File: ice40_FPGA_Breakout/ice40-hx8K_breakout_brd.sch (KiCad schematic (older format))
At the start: 0 parts

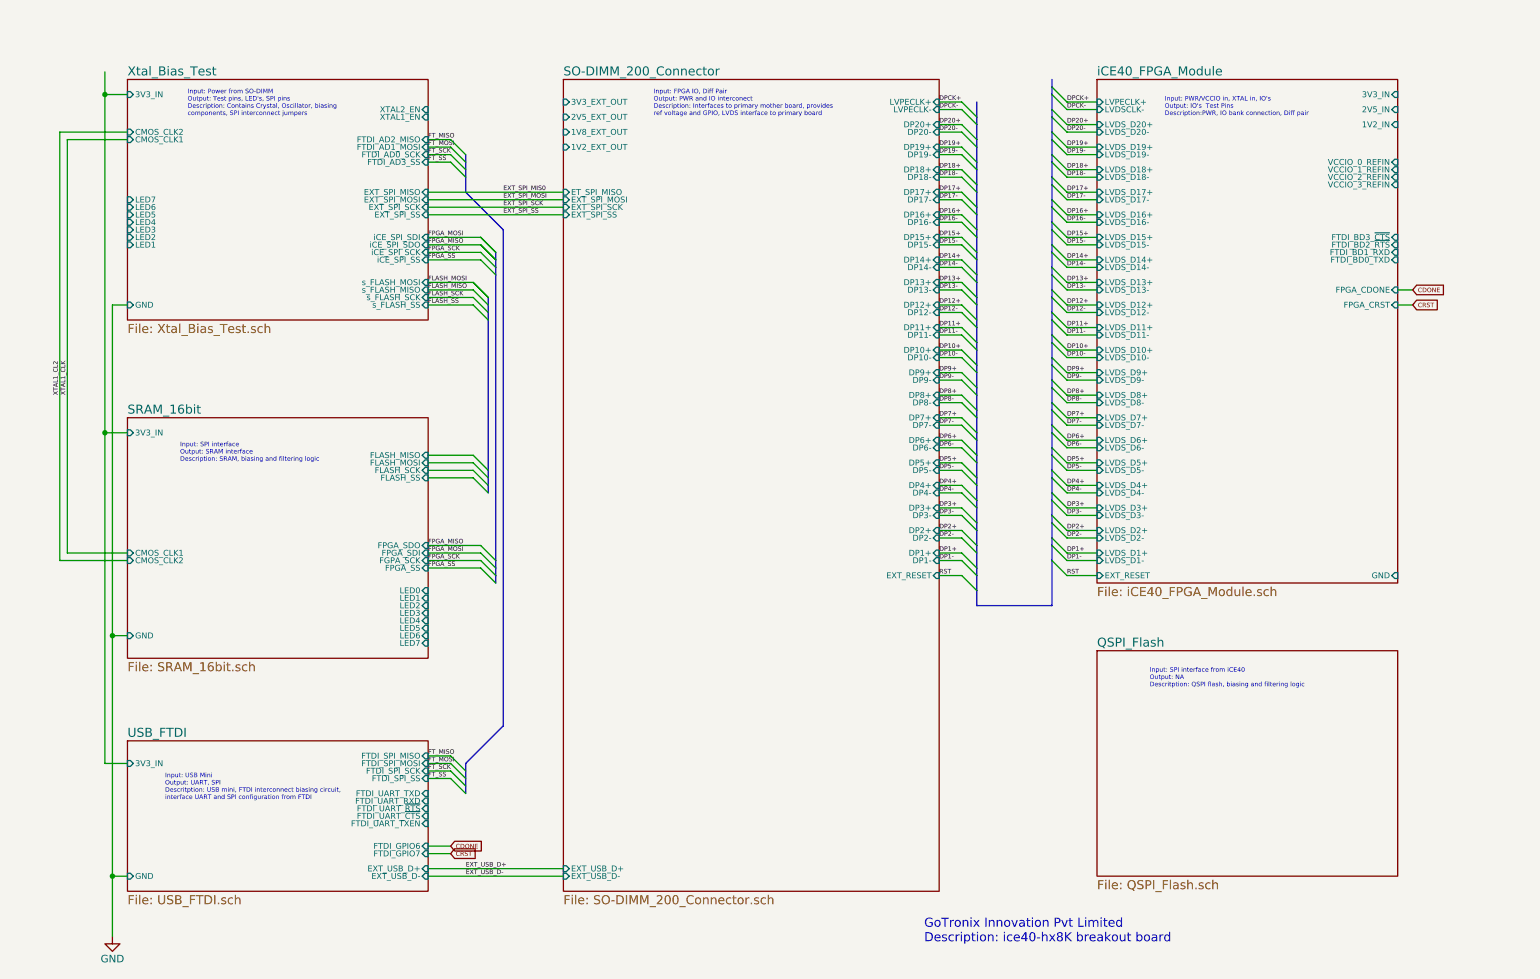
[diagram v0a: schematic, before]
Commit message: memory modules added
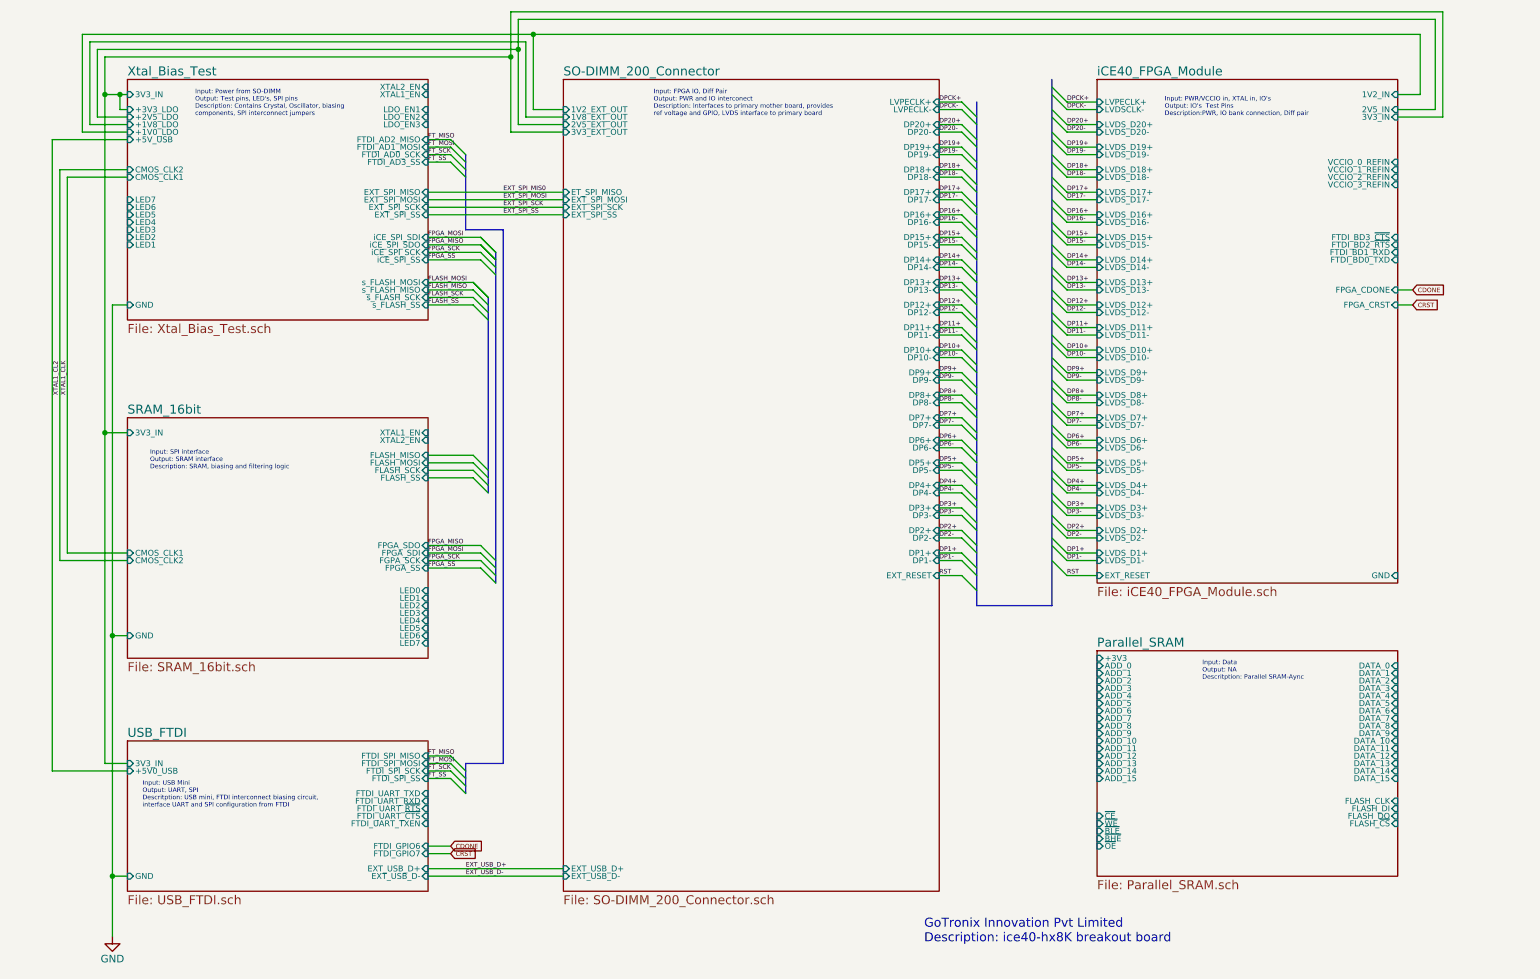
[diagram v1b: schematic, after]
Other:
- note added: "Input: Data\nOutput: NA\nDescritption: Parallel SRAM-Aync"
- note removed: "Input: SPI interface from iCE40\nOutput: NA\nDescritption: QSPI flash, biasing and filtering logic"

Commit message: fix based on feedback and decoupluing caps added
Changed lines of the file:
@@
 F42 "FLASH_DO" I R 10150 5900 39
 F43 "FLASH_~CS" I R 10150 5950 39
+F44 "FLASH_~WP" I R 10150 6000 39
+F45 "FLASH_~HOLD" I R 10150 6050 39
 $EndSheet
 $Sheet
@@
 	7350 1150 7350 4500
 Wire Bus Line
-	7850 4500 7350 4500
+	7350 4500 7850 4500
 Wire Bus Line
-	7850 1000 7850 4500
+	7850 4500 7850 1000
 Wire Wire Line
 	7950 1150 8150 1150
@@
 Connection ~ 1650 1100
 Wire Wire Line
-	1550 850  4250 850
+	1200 850  4250 850
 Wire Wire Line
 	4250 550  4250 1350
@@
 	10150 1250 10450 1250
 Wire Wire Line
-	10450 550  10450 1250
-Wire Wire Line
-	4250 550  10450 550
+	10450 1250 10450 550
+Wire Wire Line
+	10450 550  4250 550
 Connection ~ 4250 850
+Text GLabel 1200 850  0    39   Input ~ 0
++3V3
+Connection ~ 1550 850
+Wire Wire Line
+	8150 4850 8050 4850
+Text GLabel 8050 4850 0    39   Input ~ 0
++3V3
 $EndSCHEMATC

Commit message: post review fix
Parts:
- added R? (x12): R, symbol R
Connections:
- net +3V3: now also R?.1, R?.1, R?.2, R?.2
- net iCE40_FPGA_Module/VCCIO_0_REFIN: now also R?.1, R?.1, R?.1
- net iCE40_FPGA_Module/VCCIO_1_REFIN: now also R?.1, R?.1, R?.1
- net iCE40_FPGA_Module/VCCIO_2_REFIN: now also R?.2, R?.2, R?.2
- net iCE40_FPGA_Module/VCCIO_3_REFIN: now also R?.2, R?.2, R?.2
- new net +1V8: R?.1, R?.1, R?.2, R?.2
- new net +2V5: R?.1, R?.1, R?.2, R?.2

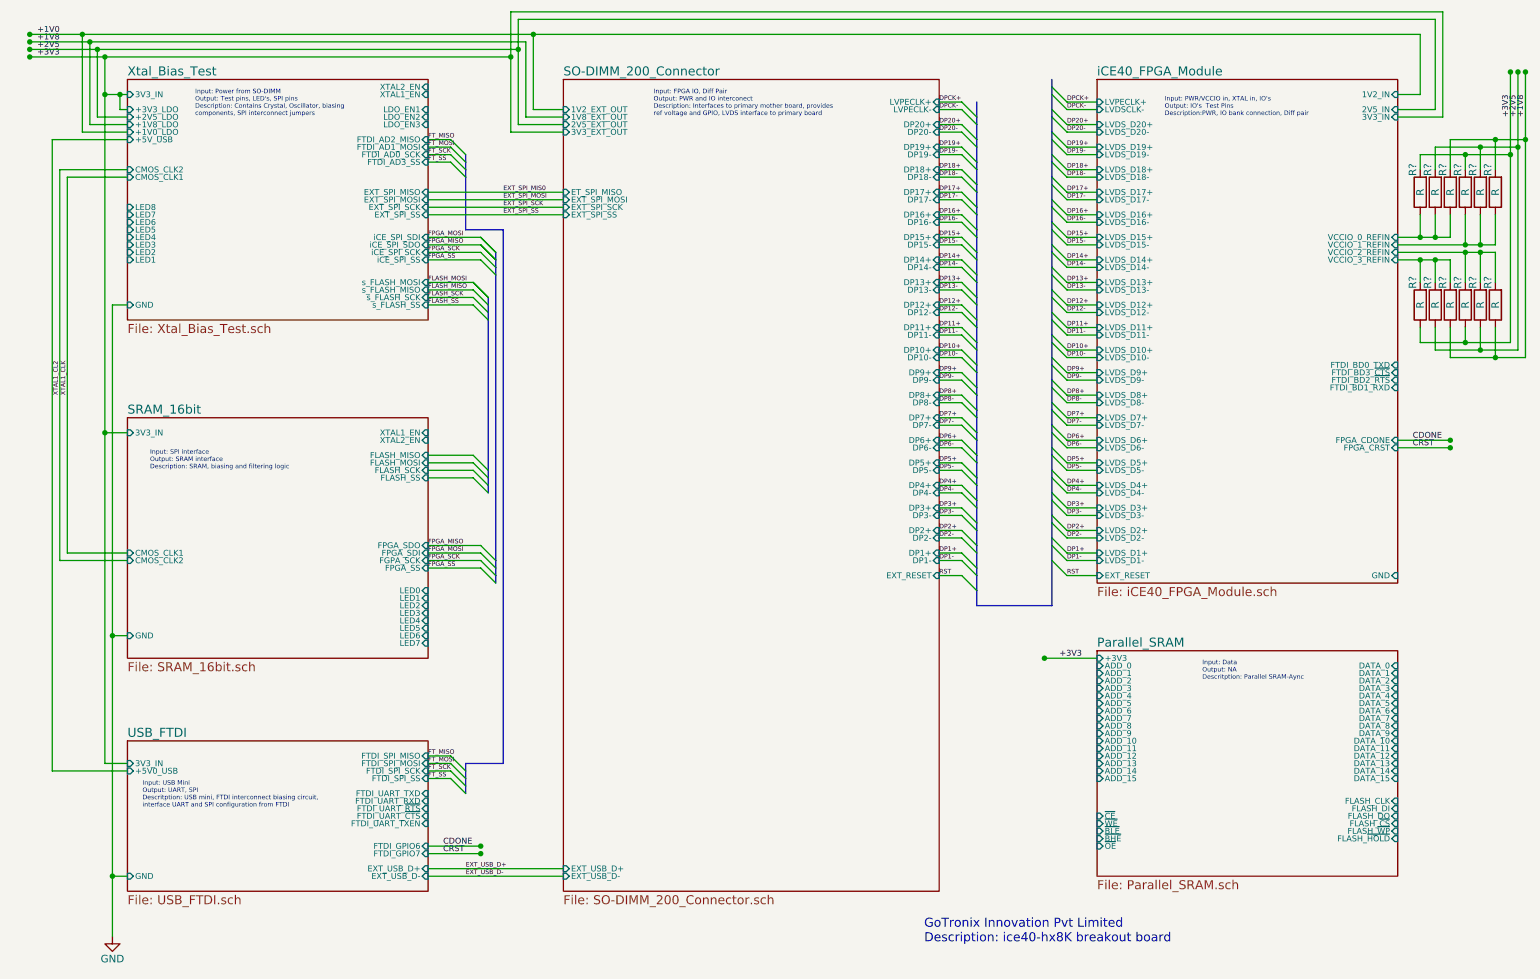
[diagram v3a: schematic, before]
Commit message: added shotkey diode to FPGA 1.2V
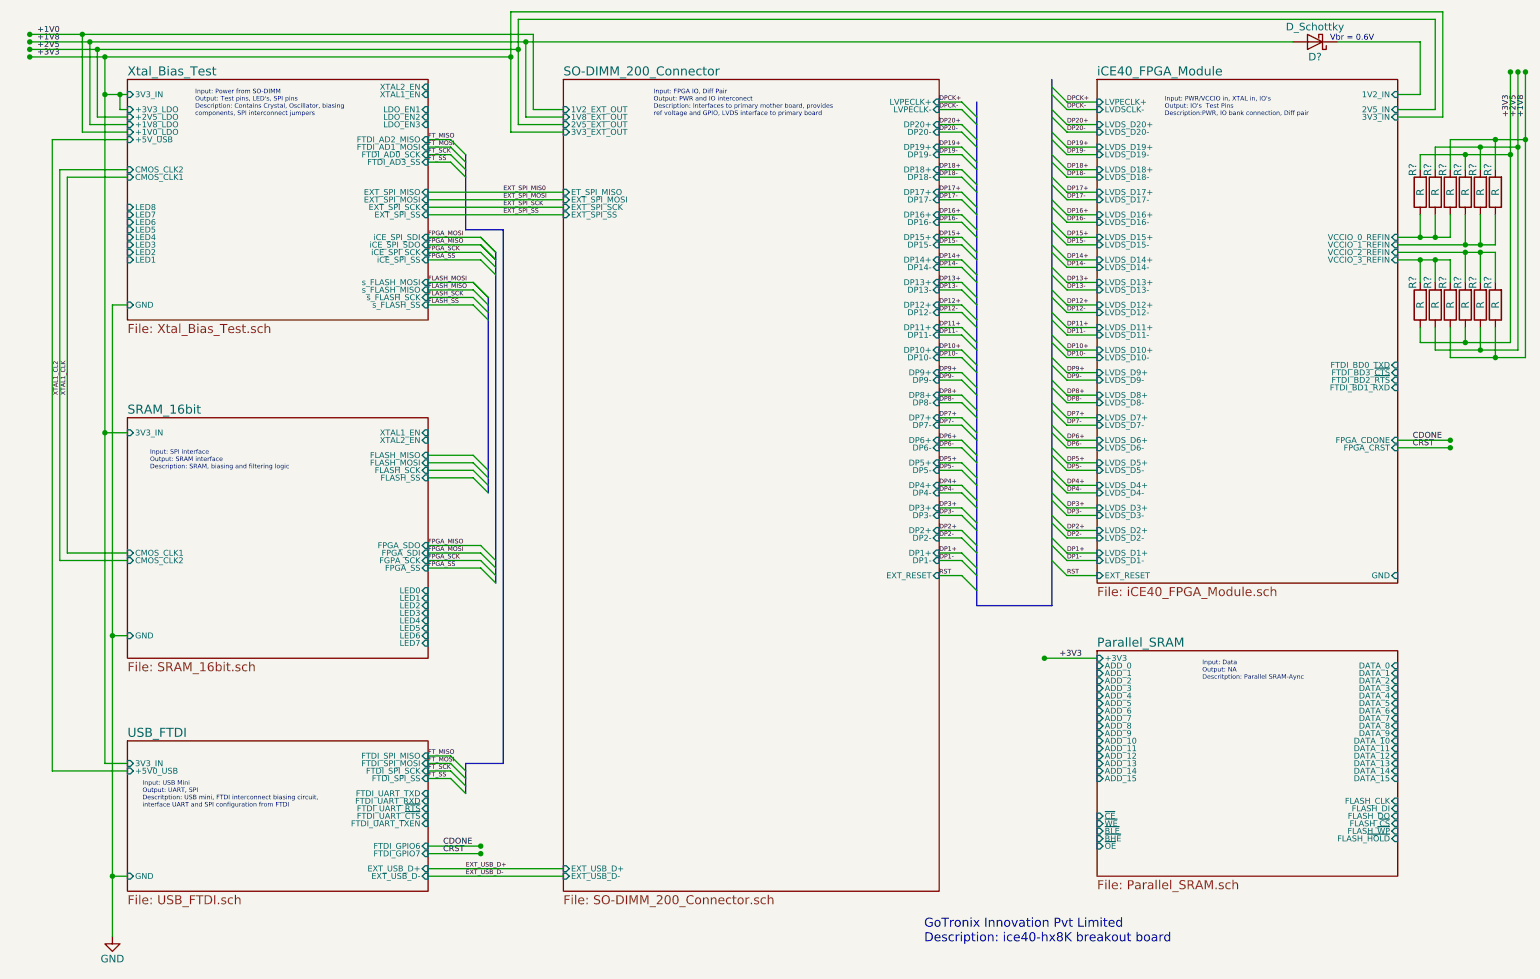
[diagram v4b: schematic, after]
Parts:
- added D?: D_Schottky, symbol D_Schottky
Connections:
- net +1V8: now also D?.2 (A)
- new net iCE40_FPGA_Module/1V2_IN: D?.1 (K)
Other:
- note added: "Vbr = 0.6V"

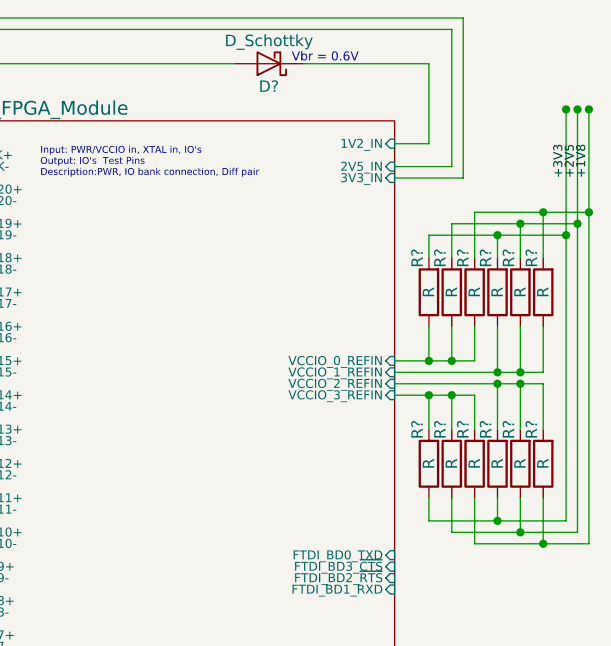
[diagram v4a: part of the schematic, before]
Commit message: Component Annotated and R/C/Conn/TP CVPCB mapping
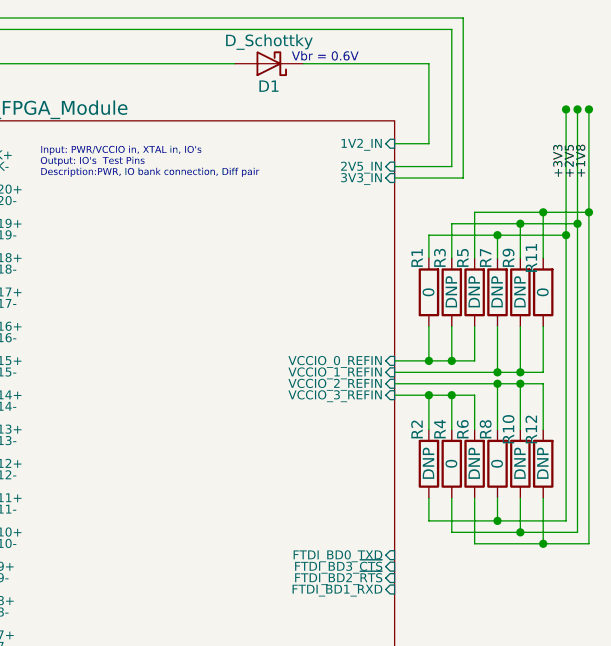
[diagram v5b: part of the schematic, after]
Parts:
- R1, R11, R4, R8: renamed from R?; value R -> 0
- R10, R12, R2, R3, R5, R6, R7, R9: renamed from R?; value R -> DNP
- gave numbers to parts that had none: 1
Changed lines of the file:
@@
 FPGA_SS
 $Comp
-L R R?
+L R R1
 U 1 1 5A61EAF8
 P 10300 1750
-F 0 "R?" V 10350 1600 50  0000 C CNN
-F 1 "R" V 10300 1750 50  0000 C CNN
+F 0 "R1" V 10350 1600 50  0000 C CNN
+F 1 "0" V 10300 1750 50  0000 C CNN
 F 2 "" V 10230 1750 50  0001 C CNN
 F 3 "" H 10300 1750 50  0001 C CNN
@@
 $EndComp
 $Comp
-L R R?
+L R R3
 U 1 1 5A62B56E
 P 10400 1750
-F 0 "R?" V 10450 1600 50  0000 C CNN
-F 1 "R" V 10400 1750 50  0000 C CNN
+F 0 "R3" V 10450 1600 50  0000 C CNN
+F 1 "DNP" V 10400 1750 50  0000 C CNN
 F 2 "" V 10330 1750 50  0001 C CNN
 F 3 "" H 10400 1750 50  0001 C CNN
@@
 $EndComp
 $Comp
-L R R?
+L R R5
 U 1 1 5A62BAEE
 P 10500 1750
-F 0 "R?" V 10550 1600 50  0000 C CNN
-F 1 "R" V 10500 1750 50  0000 C CNN
+F 0 "R5" V 10550 1600 50  0000 C CNN
+F 1 "DNP" V 10500 1750 50  0000 C CNN
 F 2 "" V 10430 1750 50  0001 C CNN
 F 3 "" H 10500 1750 50  0001 C CNN
@@
 $EndComp
 $Comp
-L R R?
+L R R7
 U 1 1 5A62C079
 P 10600 1750
-F 0 "R?" V 10650 1600 50  0000 C CNN
-F 1 "R" V 10600 1750 50  0000 C CNN
+F 0 "R7" V 10650 1600 50  0000 C CNN
+F 1 "DNP" V 10600 1750 50  0000 C CNN
 F 2 "" V 10530 1750 50  0001 C CNN
 F 3 "" H 10600 1750 50  0001 C CNN
@@
 $EndComp
 $Comp
-L R R?
+L R R9
 U 1 1 5A63AC19
 P 10700 1750
-F 0 "R?" V 10750 1600 50  0000 C CNN
-F 1 "R" V 10700 1750 50  0000 C CNN
+F 0 "R9" V 10750 1600 50  0000 C CNN
+F 1 "DNP" V 10700 1750 50  0000 C CNN
 F 2 "" V 10630 1750 50  0001 C CNN
 F 3 "" H 10700 1750 50  0001 C CNN
@@
 $EndComp
 $Comp
-L R R?
+L R R11
 U 1 1 5A63B1A0
 P 10800 1750
-F 0 "R?" V 10850 1600 50  0000 C CNN
-F 1 "R" V 10800 1750 50  0000 C CNN
+F 0 "R11" V 10850 1600 50  0000 C CNN
+F 1 "0" V 10800 1750 50  0000 C CNN
 F 2 "" V 10730 1750 50  0001 C CNN
 F 3 "" H 10800 1750 50  0001 C CNN
@@
 $EndComp
 $Comp
-L R R?
+L R R8
 U 1 1 5A63B732
 P 10600 2500
-F 0 "R?" V 10650 2350 50  0000 C CNN
-F 1 "R" V 10600 2500 50  0000 C CNN
+F 0 "R8" V 10650 2350 50  0000 C CNN
+F 1 "0" V 10600 2500 50  0000 C CNN
 F 2 "" V 10530 2500 50  0001 C CNN
 F 3 "" H 10600 2500 50  0001 C CNN
@@
 $EndComp
 $Comp
-L R R?
+L R R10
 U 1 1 5A63BCC3
 P 10700 2500
-F 0 "R?" V 10750 2350 50  0000 C CNN
-F 1 "R" V 10700 2500 50  0000 C CNN
+F 0 "R10" V 10750 2350 50  0000 C CNN
+F 1 "DNP" V 10700 2500 50  0000 C CNN
 F 2 "" V 10630 2500 50  0001 C CNN
 F 3 "" H 10700 2500 50  0001 C CNN
@@
 $EndComp
 $Comp
-L R R?
+L R R12
 U 1 1 5A63C25B
 P 10800 2500
-F 0 "R?" V 10850 2350 50  0000 C CNN
-F 1 "R" V 10800 2500 50  0000 C CNN
+F 0 "R12" V 10850 2350 50  0000 C CNN
+F 1 "DNP" V 10800 2500 50  0000 C CNN
 F 2 "" V 10730 2500 50  0001 C CNN
 F 3 "" H 10800 2500 50  0001 C CNN
@@
 $EndComp
 $Comp
-L R R?
+L R R2
 U 1 1 5A6400C0
 P 10300 2500
-F 0 "R?" V 10350 2350 50  0000 C CNN
-F 1 "R" V 10300 2500 50  0000 C CNN
+F 0 "R2" V 10350 2350 50  0000 C CNN
+F 1 "DNP" V 10300 2500 50  0000 C CNN
 F 2 "" V 10230 2500 50  0001 C CNN
 F 3 "" H 10300 2500 50  0001 C CNN
@@
 $EndComp
 $Comp
-L R R?
+L R R4
 U 1 1 5A640686
 P 10400 2500
-F 0 "R?" V 10450 2350 50  0000 C CNN
-F 1 "R" V 10400 2500 50  0000 C CNN
+F 0 "R4" V 10450 2350 50  0000 C CNN
+F 1 "0" V 10400 2500 50  0000 C CNN
 F 2 "" V 10330 2500 50  0001 C CNN
 F 3 "" H 10400 2500 50  0001 C CNN
@@
 $EndComp
 $Comp
-L R R?
+L R R6
 U 1 1 5A640C1D
 P 10500 2500
-F 0 "R?" V 10550 2350 50  0000 C CNN
-F 1 "R" V 10500 2500 50  0000 C CNN
+F 0 "R6" V 10550 2350 50  0000 C CNN
+F 1 "DNP" V 10500 2500 50  0000 C CNN
 F 2 "" V 10430 2500 50  0001 C CNN
 F 3 "" H 10500 2500 50  0001 C CNN
@@
 	10150 1200 10400 1200
 $Comp
-L D_Schottky D?
+L D_Schottky D1
 U 1 1 5A6D3B22
 P 9600 750
-F 0 "D?" H 9600 850 50  0000 C CNN
+F 0 "D1" H 9600 850 50  0000 C CNN
 F 1 "D_Schottky" H 9600 650 50  0000 C CNN
 F 2 "" H 9600 750 50  0001 C CNN

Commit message: schematic clean up, label aligned
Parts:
- R1, R10, R11, R12, R2, R3, R4, R5, R6, R7, R8, R9: footprint (none) -> Resistor_SMD:R_0603_1608Metric
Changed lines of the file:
@@
 F 0 "R1" V 10350 1600 50  0000 C CNN
 F 1 "0" V 10300 1750 50  0000 C CNN
-F 2 "" V 10230 1750 50  0001 C CNN
+F 2 "Resistor_SMD:R_0603_1608Metric" V 10230 1750 50  0001 C CNN
 F 3 "" H 10300 1750 50  0001 C CNN
 	1    10300 1750
@@
 F 0 "R3" V 10450 1600 50  0000 C CNN
 F 1 "DNP" V 10400 1750 50  0000 C CNN
-F 2 "" V 10330 1750 50  0001 C CNN
+F 2 "Resistor_SMD:R_0603_1608Metric" V 10330 1750 50  0001 C CNN
 F 3 "" H 10400 1750 50  0001 C CNN
 	1    10400 1750
@@
 F 0 "R5" V 10550 1600 50  0000 C CNN
 F 1 "DNP" V 10500 1750 50  0000 C CNN
-F 2 "" V 10430 1750 50  0001 C CNN
+F 2 "Resistor_SMD:R_0603_1608Metric" V 10430 1750 50  0001 C CNN
 F 3 "" H 10500 1750 50  0001 C CNN
 	1    10500 1750
@@
 F 0 "R7" V 10650 1600 50  0000 C CNN
 F 1 "DNP" V 10600 1750 50  0000 C CNN
-F 2 "" V 10530 1750 50  0001 C CNN
+F 2 "Resistor_SMD:R_0603_1608Metric" V 10530 1750 50  0001 C CNN
 F 3 "" H 10600 1750 50  0001 C CNN
 	1    10600 1750
@@
 F 0 "R9" V 10750 1600 50  0000 C CNN
 F 1 "DNP" V 10700 1750 50  0000 C CNN
-F 2 "" V 10630 1750 50  0001 C CNN
+F 2 "Resistor_SMD:R_0603_1608Metric" V 10630 1750 50  0001 C CNN
 F 3 "" H 10700 1750 50  0001 C CNN
 	1    10700 1750
@@
 F 0 "R11" V 10850 1600 50  0000 C CNN
 F 1 "0" V 10800 1750 50  0000 C CNN
-F 2 "" V 10730 1750 50  0001 C CNN
+F 2 "Resistor_SMD:R_0603_1608Metric" V 10730 1750 50  0001 C CNN
 F 3 "" H 10800 1750 50  0001 C CNN
 	1    10800 1750
@@
 F 0 "R8" V 10650 2350 50  0000 C CNN
 F 1 "0" V 10600 2500 50  0000 C CNN
-F 2 "" V 10530 2500 50  0001 C CNN
+F 2 "Resistor_SMD:R_0603_1608Metric" V 10530 2500 50  0001 C CNN
 F 3 "" H 10600 2500 50  0001 C CNN
 	1    10600 2500
@@
 F 0 "R10" V 10750 2350 50  0000 C CNN
 F 1 "DNP" V 10700 2500 50  0000 C CNN
-F 2 "" V 10630 2500 50  0001 C CNN
+F 2 "Resistor_SMD:R_0603_1608Metric" V 10630 2500 50  0001 C CNN
 F 3 "" H 10700 2500 50  0001 C CNN
 	1    10700 2500
@@
 F 0 "R12" V 10850 2350 50  0000 C CNN
 F 1 "DNP" V 10800 2500 50  0000 C CNN
-F 2 "" V 10730 2500 50  0001 C CNN
+F 2 "Resistor_SMD:R_0603_1608Metric" V 10730 2500 50  0001 C CNN
 F 3 "" H 10800 2500 50  0001 C CNN
 	1    10800 2500
@@
 F 0 "R2" V 10350 2350 50  0000 C CNN
 F 1 "DNP" V 10300 2500 50  0000 C CNN
-F 2 "" V 10230 2500 50  0001 C CNN
+F 2 "Resistor_SMD:R_0603_1608Metric" V 10230 2500 50  0001 C CNN
 F 3 "" H 10300 2500 50  0001 C CNN
 	1    10300 2500
@@
 F 0 "R4" V 10450 2350 50  0000 C CNN
 F 1 "0" V 10400 2500 50  0000 C CNN
-F 2 "" V 10330 2500 50  0001 C CNN
+F 2 "Resistor_SMD:R_0603_1608Metric" V 10330 2500 50  0001 C CNN
 F 3 "" H 10400 2500 50  0001 C CNN
 	1    10400 2500
@@
 F 0 "R6" V 10550 2350 50  0000 C CNN
 F 1 "DNP" V 10500 2500 50  0000 C CNN
-F 2 "" V 10430 2500 50  0001 C CNN
+F 2 "Resistor_SMD:R_0603_1608Metric" V 10430 2500 50  0001 C CNN
 F 3 "" H 10500 2500 50  0001 C CNN
 	1    10500 2500

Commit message: assigned footprint to each component
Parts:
- D1: value D_Schottky -> CDBW140-G; footprint (none) -> Diode_SMD:D_SOD-123
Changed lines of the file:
@@
 P 9600 750
 F 0 "D1" H 9600 850 50  0000 C CNN
-F 1 "D_Schottky" H 9600 650 50  0000 C CNN
-F 2 "" H 9600 750 50  0001 C CNN
+F 1 "CDBW140-G" H 9600 650 50  0000 C CNN
+F 2 "Diode_SMD:D_SOD-123" H 9600 750 50  0001 C CNN
 F 3 "" H 9600 750 50  0001 C CNN
 	1    9600 750
